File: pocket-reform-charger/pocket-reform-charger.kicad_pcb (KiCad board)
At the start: 2 copper layers, 41 x 65.5 mm, 63 parts, among them J1 CHARGER, Q1 IRF7458TRPBF, Q2 IRF7458TRPBF, U1 MP2650, U2 MAX17320G20+

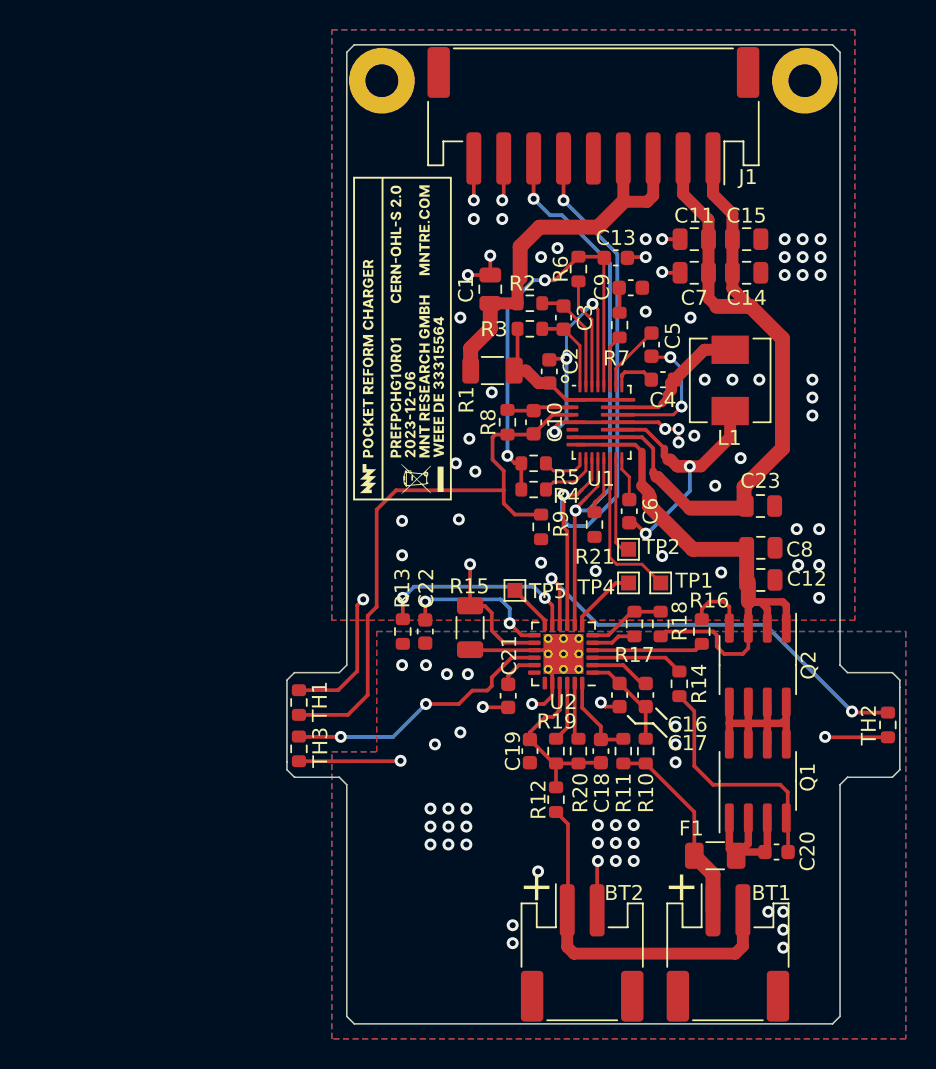
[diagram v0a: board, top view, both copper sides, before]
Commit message: charger: v2 WIP
* new 4 layer design
* optimized current flow
* better sense layout
* actually have smth worthy of being called a ground plane

missing:
* NX20P5090UKAZ
* routing of I/O signals
* proper kelvin footprint
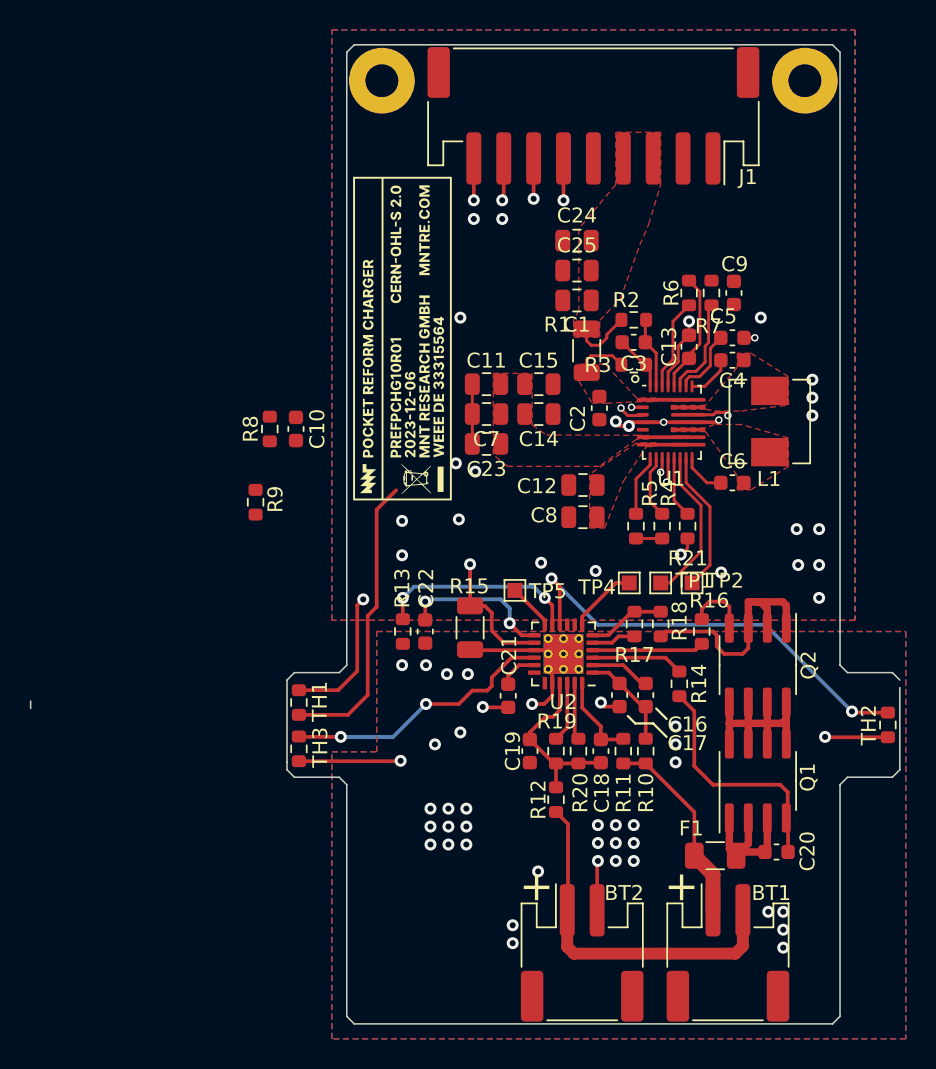
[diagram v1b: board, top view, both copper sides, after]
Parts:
- added C24: 22uF, Capacitor_SMD:C_0805_2012Metric, F.Cu at (99.4, 77.1)
- added C25: 22uF, Capacitor_SMD:C_0805_2012Metric, F.Cu at (99.4, 79.1)
- moved R9 19.2 mm to (77.9, 94.6)
- moved C23 18.8 mm to (93.3, 90.7), turned to 180 degrees
- moved C11 16.9 mm to (93.3, 86.7)
- moved C15 16.9 mm to (96.8, 86.7)
- moved C14 16.8 mm to (96.8, 88.7)
- moved C7 16.8 mm to (93.3, 88.7)
- moved C10 15.9 mm to (80.6, 89.7)
- moved R8 15.9 mm to (78.8, 89.7)
- moved C12 13.5 mm to (99.8, 93.5), turned to 180 degrees
- moved C8 12.1 mm to (99.8, 95.6), turned to 180 degrees
- moved R4 8.94 mm to (105.1, 96.2), turned to 90 degrees
- moved R5 8.04 mm to (103.3, 96.2), turned to 90 degrees
- moved C13 7.71 mm to (106.9, 84.2), turned to 90 degrees
- moved R6 7.57 mm to (106.9, 80.6)
- moved R3 7.35 mm to (103.2, 85.4)
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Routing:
- net SYSPOWER: track 53.9 -> 3.05 mm
- net I2C_SDA: track 43.0 -> 3.79 mm
- net I2C_SCL: track 39.4 -> 4.34 mm
- net CHGPOWER: track 26.4 -> 4.09 mm
- net 3V6: track 29.4 -> 9.84 mm, vias 2 -> 0
- net Net-(U1-SW2): track 19.4 -> 0.00 mm, vias 2 -> 0
- net Net-(U1-NTC): track 40.4 -> 21.3 mm, vias 0 -> 1
- net /PACK+: track 36.6 -> 19.5 mm
- net GND: track 56.7 -> 41.2 mm, vias 57 -> 30
- net Net-(U1-SW1): track 9.55 -> 0.00 mm
- net Net-(U1-CP1): track 9.38 -> 3.52 mm
- net Net-(C2-Pad2): track 10.6 -> 6.32 mm
- net Net-(U1-VNTC): track 4.46 -> 0.75 mm, vias 0 -> 1
- net Net-(U1-VMAX_BST): track 3.54 -> 6.63 mm
- net Net-(U1-IAM): track 6.69 -> 9.51 mm
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- added copper zone on F.Cu, net /PACK+
- added copper zone on F.Cu, net CHGPOWER
- added copper zone on In1.Cu, net GND
- added copper zone on F.Cu, net Net-(C2-Pad2)
- added copper zone on F.Cu, net Net-(U1-SW1)
- added copper zone on F.Cu, net Net-(U1-SW2)
- added copper zone on F.Cu, net SYSPOWER
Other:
- board size 41 x 65.5 mm -> 58.1 x 65.5 mm
- copper layers 2 -> 4

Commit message: charger: v2 WIP
* changed IRF FETs to cheaper diodes dual FET
* Add NXP 20P5090 OVP / slew rate limiter

missing:
* SYSPOWER routing to J1
* I2C, NTC filtering
* review of MAX17320G20+ protection layout
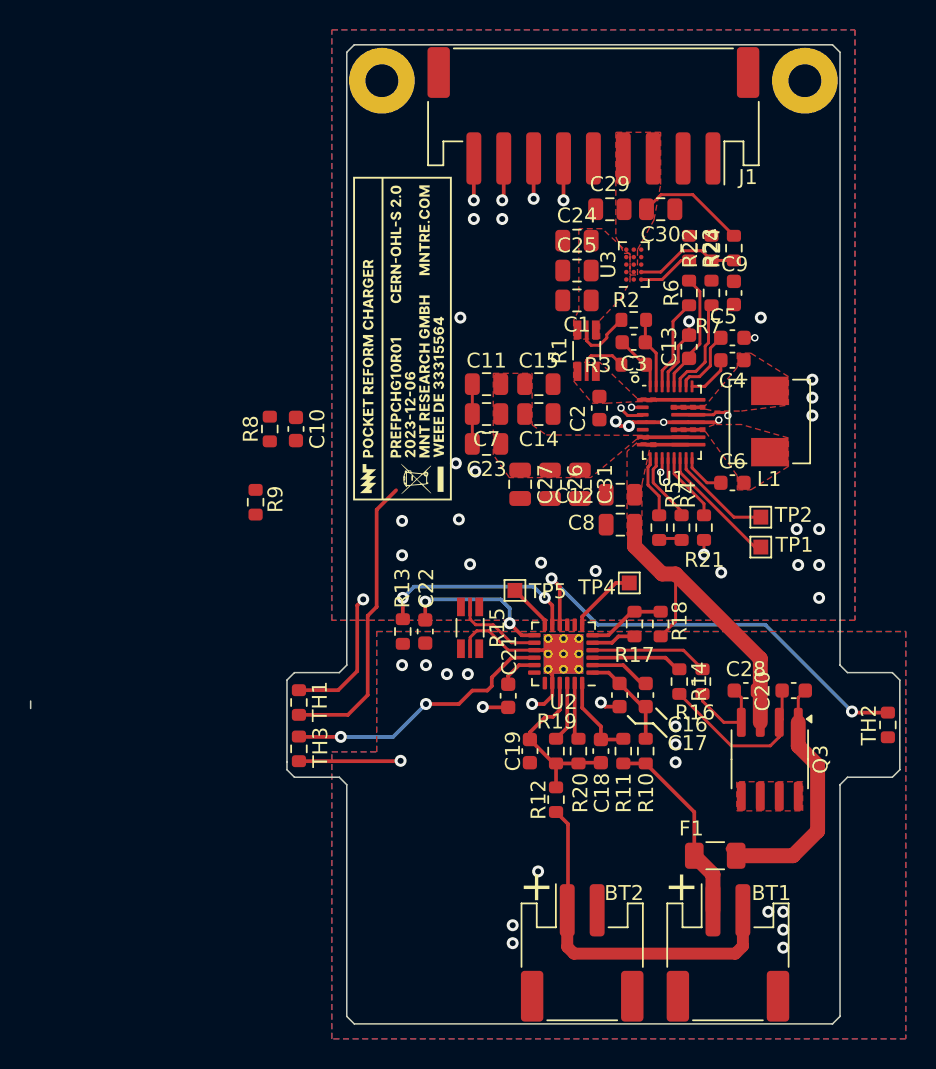
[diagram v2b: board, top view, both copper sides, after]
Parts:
- removed Q1, Q2: IRF7458TRPBF, Package_SO:SOIC-8_3.9x4.9mm_P1.27mm
- added C26: 22uF, Capacitor_SMD:C_0805_2012Metric, F.Cu at (97.6, 93.4)
- added C27: 22uF, Capacitor_SMD:C_0805_2012Metric, F.Cu at (95.6, 93.4)
- added C28: 0.1uF, Capacitor_SMD:C_0603_1608Metric, F.Cu at (110.7, 107.2)
- added C29: 22uF, Capacitor_SMD:C_0805_2012Metric, F.Cu at (101.6, 75.0)
- added C30: 22uF, Capacitor_SMD:C_0805_2012Metric, F.Cu at (105.0, 75.0)
- added C31: 22uF, Capacitor_SMD:C_0805_2012Metric, F.Cu at (99.6, 93.4)
- added Q3: Q_Dual_NMOS_S1G1S2G2D2D2D1D1, Package_SO:SOIC-8_3.9x4.9mm_P1.27mm, F.Cu at (112.3, 111.8)
- added R22: 0, Resistor_SMD:R_0603_1608Metric, F.Cu at (108.4, 77.6)
- added R23: 100k, Resistor_SMD:R_0603_1608Metric, F.Cu at (106.9, 77.6)
- added R24: 100k, Resistor_SMD:R_0603_1608Metric, F.Cu at (109.9, 77.6)
- added U3: NX20P5090, pocket-reform-charger:NXP_NX20P5090, F.Cu at (103.2, 78.7)
- R1, R15: footprint Resistor_SMD:R_1206_3216Metric -> pocket-reform-charger:R_1206_3216Metric_Kelvin
- moved C20 10.9 mm to (113.9, 107.2), turned to 0 degrees
- moved TP1 7.12 mm to (111.7, 97.6)
- moved TP2 6.37 mm to (111.7, 95.6)
- moved R16 3.35 mm to (107.8, 106.6), turned to -90 degrees
- moved C12 2.58 mm to (102.3, 94.1)
- moved C8 2.55 mm to (102.3, 96.1)
- moved R5 1.55 mm to (104.9, 96.3)
- moved R4 1.30 mm to (106.4, 96.3)
- moved R21 1.10 mm to (107.9, 96.3)
- moved R14 0.15 mm to (106.2, 106.6)
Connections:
- C1 pad 2: CHGPOWER -> CHGPOWER_PROT
- C24 pad 2: CHGPOWER -> CHGPOWER_PROT
- C25 pad 2: CHGPOWER -> CHGPOWER_PROT
- R1 pad 2: CHGPOWER -> Net-(R1-Pad2)
- R15 pad 2: PACKGND -> Net-(U2-CSN)
- R2 pad 2: CHGPOWER -> Net-(R1-Pad3)
- R3 pad 2: Net-(C2-Pad2) -> Net-(R1-Pad2)
- U2 pad 14: GND -> Net-(U2-CSN)
- U2 pad 15: PACKGND -> Net-(U2-CSP)
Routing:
- net Net-(Q1-D-Pad5): track 15.1 -> 0.00 mm
- net PACKGND: track 26.2 -> 14.3 mm, vias 39 -> 18
- net GND: track 41.2 -> 32.1 mm, vias 30 -> 29
- net Net-(Q3A-S): track 9.95 -> 17.3 mm
- net Net-(U3-OVLO): track 0.00 -> 7.06 mm
- net Net-(U2-CSN): track 0.00 -> 5.78 mm
- net Net-(U2-CSP): track 0.00 -> 5.40 mm
- net /PACK+: track 19.5 -> 24.6 mm
- net Net-(Q3A-G): track 16.2 -> 11.6 mm
- net Net-(R1-Pad3): track 0.00 -> 4.09 mm
- net Net-(U3-~{EN}): track 0.00 -> 3.73 mm
- net Net-(C2-Pad2): track 6.32 -> 2.80 mm
- net Net-(R1-Pad2): track 0.00 -> 3.52 mm
- net CHGPOWER: track 4.09 -> 7.39 mm
- net Net-(U1-IAM): track 9.51 -> 7.08 mm
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- added copper zone on F.Cu, net CHGPOWER_PROT
- added copper zone on F.Cu, net Net-(Q3A-D-Pad7)
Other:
- outline, holes or cut-outs redrawn

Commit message: pocket-reform-charger pcb v2 layout completed
- layout finished by carson walls
- initial new mp2650+nx20p5090 layout by f. schneider
- final polishing by lucie l. hartmann

Co-authored-by: Carson Walls <carson@decapoddevices.com>
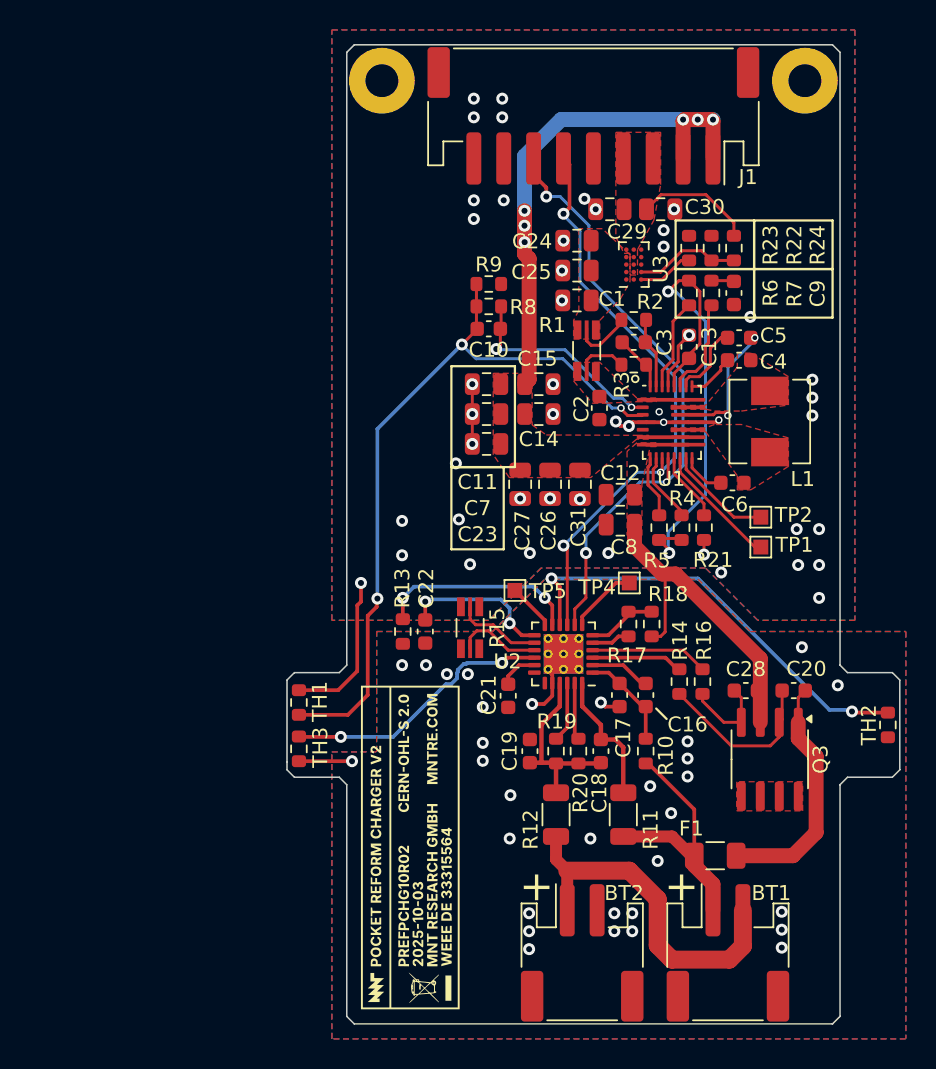
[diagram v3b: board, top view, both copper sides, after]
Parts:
- R11, R12: footprint Resistor_SMD:R_0603_1608Metric -> Resistor_SMD:R_1206_3216Metric
- moved H5 34.0 mm to (88.2, 117.7)
- moved R9 21.4 mm to (93.5, 80.0), turned to 0 degrees
- moved R8 16.8 mm to (93.5, 81.5), turned to 180 degrees
- moved C10 14.5 mm to (93.5, 83.0), turned to 180 degrees
- moved R11 4.25 mm to (102.5, 115.5)
- moved R12 1.00 mm to (98.0, 115.5)
- moved R18 0.60 mm to (104.4, 102.8)
- moved C4 0.45 mm to (110.2, 85.1)
- moved C5 0.45 mm to (110.2, 83.6)
- moved R17 0.40 mm to (102.8, 102.8)
- turned C19 to -90 degrees
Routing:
- net SYSPOWER: track 3.05 -> 41.4 mm, vias 1 -> 6
- net I2C_SCL: track 4.34 -> 41.6 mm, vias 2 -> 3
- net I2C_SDA: track 3.79 -> 39.8 mm, vias 2 -> 3
- net Net-(U1-NTC): track 21.3 -> 49.8 mm, vias 1 -> 3
- net 3V6: track 9.67 -> 32.4 mm, vias 0 -> 2
- net Net-(U1-VNTC): track 0.75 -> 14.4 mm, vias 1 -> 2
- net PACKGND: track 14.3 -> 8.39 mm, vias 18 -> 31
- net GND: track 32.1 -> 26.6 mm, vias 29 -> 48
- net Net-(U1-CP1): track 3.52 -> 9.02 mm
- net Net-(BT1-+): track 13.2 -> 17.1 mm
- net Net-(U2-BATTS): track 5.81 -> 9.05 mm
- net Net-(C9-Pad2): track 0.00 -> 1.52 mm
- net /PACK+: track 24.6 -> 25.6 mm
- net Net-(Q3A-S): track 17.3 -> 16.5 mm
- net Net-(U2-CELL1): track 11.9 -> 12.6 mm
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- added copper zone on In2.Cu, net GND
- added copper zone on In1.Cu, net PACKGND
- added copper zone on In2.Cu, net PACKGND
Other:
- board size 58.1 x 65.5 mm -> 41 x 65.5 mm
